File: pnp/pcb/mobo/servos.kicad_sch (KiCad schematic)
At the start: 3 parts, among them J15 SERVO1, J16 SERVO2, U7 SN74LVC2G34

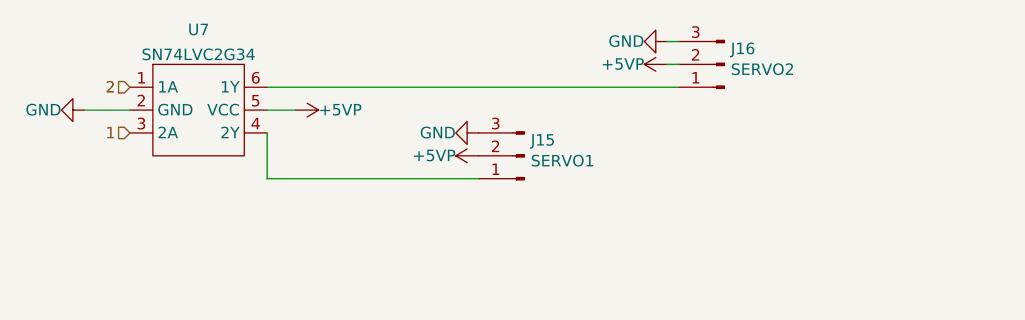
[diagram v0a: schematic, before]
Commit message: Mobo V4A Redesign
Some EMC improvements to schematics.
Reassigned MCU Pins for HW-PWM support.
Changes are still marked with text in the schematics.
Complete PCB Layout reworked
Status: Needs to be verified, and cleaned up a little, but DRC is running green.
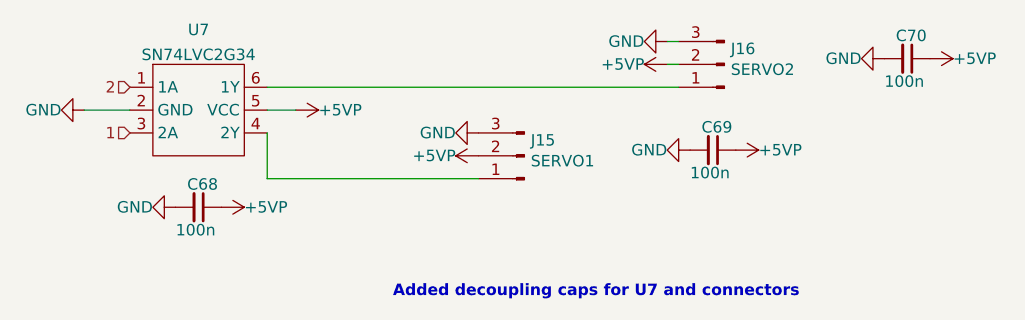
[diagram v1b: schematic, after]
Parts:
- added C68, C69, C70: 100n, Capacitor_SMD:C_0805_2012Metric, symbol Device:C_Small
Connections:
- net +5VP: now also C68.1, C69.1, C70.1
- net GND: now also C68.2, C69.2, C70.2
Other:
- note added: "Added decoupling caps for U7 and connectors"
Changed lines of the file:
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@@
   (title_block
     (title "LumenPnP Motherboard")
-    (date "2022-03-29")
+    (date "2022-09-09")
+    (rev "004A")
     (company "Opulo")
+    (comment 1 "Reengineered by Magpie")
   )
   (wire (pts (xy 119.38 108.585) (xy 142.875 108.585))
@@
   (wire (pts (xy 99.06 100.965) (xy 104.14 100.965))
     (stroke (width 0) (type default) (color 0 0 0 0))
+  )
+  (text "Added decoupling caps for U7 and connectors" (at 133.35 121.92 0)
+    (effects (font (size 1.27 1.27) (thickness 0.254) bold) (justify left bottom))
   )
   (hierarchical_label "1" (shape input) (at 104.14 103.505 180)
@@
     (effects (font (size 1.27 1.27)) (justify right))
   )
+  (symbol (lib_id "power:GND") (at 187.96 95.25 270) (unit 1)
+    (in_bom yes) (on_board yes)
+    (property "Reference" "#PWR030" (id 0) (at 181.61 95.25 0)
+      (effects (font (size 1.27 1.27)) hide)
+    )
+    (property "Value" "GND" (id 1) (at 185.42 95.25 90)
+      (effects (font (size 1.27 1.27)) (justify right))
+    )
+    (property "Footprint" "" (id 2) (at 187.96 95.25 0)
+      (effects (font (size 1.27 1.27)) hide)
+    )
+    (property "Datasheet" "" (id 3) (at 187.96 95.25 0)
+      (effects (font (size 1.27 1.27)) hide)
+    )
+    (pin "1")
+  )
   (symbol (lib_id "power:+5VP") (at 142.875 106.045 90) (unit 1)
     (in_bom yes) (on_board yes)
@@
     )
     (property "Datasheet" "" (id 3) (at 142.875 106.045 0)
+      (effects (font (size 1.27 1.27)) hide)
+    )
+    (pin "1")
+  )
+  (symbol (lib_id "power:+5VP") (at 171.45 105.41 270) (unit 1)
+    (in_bom yes) (on_board yes)
+    (property "Reference" "#PWR029" (id 0) (at 167.64 105.41 0)
+      (effects (font (size 1.27 1.27)) hide)
+    )
+    (property "Value" "+5VP" (id 1) (at 173.99 105.41 90)
+      (effects (font (size 1.27 1.27)) (justify left))
+    )
+    (property "Footprint" "" (id 2) (at 171.45 105.41 0)
+      (effects (font (size 1.27 1.27)) hide)
+    )
+    (property "Datasheet" "" (id 3) (at 171.45 105.41 0)
       (effects (font (size 1.27 1.27)) hide)
     )
@@
     (pin "1")
   )
+  (symbol (lib_id "power:GND") (at 166.37 105.41 270) (unit 1)
+    (in_bom yes) (on_board yes)
+    (property "Reference" "#PWR028" (id 0) (at 160.02 105.41 0)
+      (effects (font (size 1.27 1.27)) hide)
+    )
+    (property "Value" "GND" (id 1) (at 163.83 105.41 90)
+      (effects (font (size 1.27 1.27)) (justify right))
+    )
+    (property "Footprint" "" (id 2) (at 166.37 105.41 0)
+      (effects (font (size 1.27 1.27)) hide)
+    )
+    (property "Datasheet" "" (id 3) (at 166.37 105.41 0)
+      (effects (font (size 1.27 1.27)) hide)
+    )
+    (pin "1")
+  )
+  (symbol (lib_id "power:GND") (at 109.22 111.76 270) (unit 1)
+    (in_bom yes) (on_board yes)
+    (property "Reference" "#PWR026" (id 0) (at 102.87 111.76 0)
+      (effects (font (size 1.27 1.27)) hide)
+    )
+    (property "Value" "GND" (id 1) (at 106.68 111.76 90)
+      (effects (font (size 1.27 1.27)) (justify right))
+    )
+    (property "Footprint" "" (id 2) (at 109.22 111.76 0)
+      (effects (font (size 1.27 1.27)) hide)
+    )
+    (property "Datasheet" "" (id 3) (at 109.22 111.76 0)
+      (effects (font (size 1.27 1.27)) hide)
+    )
+    (pin "1")
+  )
+  (symbol (lib_id "Device:C_Small") (at 168.91 105.41 270) (unit 1)
+    (in_bom yes) (on_board yes)
+    (property "Reference" "C69" (id 0) (at 167.64 102.87 90)
+      (effects (font (size 1.27 1.27)) (justify left))
+    )
+    (property "Value" "100n" (id 1) (at 166.37 107.95 90)
+      (effects (font (size 1.27 1.27)) (justify left))
+    )
+    (property "Footprint" "Capacitor_SMD:C_0805_2012Metric" (id 2) (at 168.91 105.41 0)
+      (effects (font (size 1.27 1.27)) hide)
+    )
+    (property "Datasheet" "" (id 3) (at 168.91 105.41 0)
+      (effects (font (size 1.27 1.27)) hide)
+    )
+    (property "Digikey" "1276-1180-1-ND" (id 4) (at 168.91 105.41 0)
+      (effects (font (size 1.27 1.27)) hide)
+    )
+    (property "JLCPCB" "C49678" (id 5) (at 168.91 105.41 0)
+      (effects (font (size 1.27 1.27)) hide)
+    )
+    (property "LCSC" "C360619" (id 6) (at 168.91 105.41 0)
+      (effects (font (size 1.27 1.27)) hide)
+    )
+    (property "Mouser" "581-08055C104K" (id 7) (at 168.91 105.41 0)
+      (effects (font (size 1.27 1.27)) hide)
+    )
+    (pin "1")
+    (pin "2")
+  )
   (symbol (lib_id "power:GND") (at 163.83 93.345 270) (unit 1)
     (in_bom yes) (on_board yes)
@@
     (pin "1")
   )
+  (symbol (lib_id "power:+5VP") (at 114.3 111.76 270) (unit 1)
+    (in_bom yes) (on_board yes)
+    (property "Reference" "#PWR027" (id 0) (at 110.49 111.76 0)
+      (effects (font (size 1.27 1.27)) hide)
+    )
+    (property "Value" "+5VP" (id 1) (at 116.84 111.76 90)
+      (effects (font (size 1.27 1.27)) (justify left))
+    )
+    (property "Footprint" "" (id 2) (at 114.3 111.76 0)
+      (effects (font (size 1.27 1.27)) hide)
+    )
+    (property "Datasheet" "" (id 3) (at 114.3 111.76 0)
+      (effects (font (size 1.27 1.27)) hide)
+    )
+    (pin "1")
+  )
   (symbol (lib_id "power:+5VP") (at 163.83 95.885 90) (unit 1)
     (in_bom yes) (on_board yes)
@@
     (pin "1")
   )
+  (symbol (lib_id "Device:C_Small") (at 111.76 111.76 270) (unit 1)
+    (in_bom yes) (on_board yes)
+    (property "Reference" "C68" (id 0) (at 110.49 109.22 90)
+      (effects (font (size 1.27 1.27)) (justify left))
+    )
+    (property "Value" "100n" (id 1) (at 109.22 114.3 90)
+      (effects (font (size 1.27 1.27)) (justify left))
+    )
+    (property "Footprint" "Capacitor_SMD:C_0805_2012Metric" (id 2) (at 111.76 111.76 0)
+      (effects (font (size 1.27 1.27)) hide)
+    )
+    (property "Datasheet" "" (id 3) (at 111.76 111.76 0)
+      (effects (font (size 1.27 1.27)) hide)
+    )
+    (property "Digikey" "1276-1180-1-ND" (id 4) (at 111.76 111.76 0)
+      (effects (font (size 1.27 1.27)) hide)
+    )
+    (property "JLCPCB" "C49678" (id 5) (at 111.76 111.76 0)
+      (effects (font (size 1.27 1.27)) hide)
+    )
+    (property "LCSC" "C360619" (id 6) (at 111.76 111.76 0)
+      (effects (font (size 1.27 1.27)) hide)
+    )
+    (property "Mouser" "581-08055C104K" (id 7) (at 111.76 111.76 0)
+      (effects (font (size 1.27 1.27)) hide)
+    )
+    (pin "1")
+    (pin "2")
+  )
   (symbol (lib_id "Connector:Conn_01x03_Male") (at 170.18 95.885 180) (unit 1)
     (in_bom yes) (on_board yes)
@@
     (pin "3")
   )
+  (symbol (lib_id "power:+5VP") (at 193.04 95.25 270) (unit 1)
+    (in_bom yes) (on_board yes)
+    (property "Reference" "#PWR031" (id 0) (at 189.23 95.25 0)
+      (effects (font (size 1.27 1.27)) hide)
+    )
+    (property "Value" "+5VP" (id 1) (at 195.58 95.25 90)
+      (effects (font (size 1.27 1.27)) (justify left))
+    )
+    (property "Footprint" "" (id 2) (at 193.04 95.25 0)
+      (effects (font (size 1.27 1.27)) hide)
+    )
+    (property "Datasheet" "" (id 3) (at 193.04 95.25 0)
+      (effects (font (size 1.27 1.27)) hide)
+    )
+    (pin "1")
+  )
+  (symbol (lib_id "Device:C_Small") (at 190.5 95.25 270) (unit 1)
+    (in_bom yes) (on_board yes)
+    (property "Reference" "C70" (id 0) (at 189.23 92.71 90)
+      (effects (font (size 1.27 1.27)) (justify left))
+    )
+    (property "Value" "100n" (id 1) (at 187.96 97.79 90)
+      (effects (font (size 1.27 1.27)) (justify left))
+    )
+    (property "Footprint" "Capacitor_SMD:C_0805_2012Metric" (id 2) (at 190.5 95.25 0)
+      (effects (font (size 1.27 1.27)) hide)
+    )
+    (property "Datasheet" "" (id 3) (at 190.5 95.25 0)
+      (effects (font (size 1.27 1.27)) hide)
+    )
+    (property "Digikey" "1276-1180-1-ND" (id 4) (at 190.5 95.25 0)
+      (effects (font (size 1.27 1.27)) hide)
+    )
+    (property "JLCPCB" "C49678" (id 5) (at 190.5 95.25 0)
+      (effects (font (size 1.27 1.27)) hide)
+    )
+    (property "LCSC" "C360619" (id 6) (at 190.5 95.25 0)
+      (effects (font (size 1.27 1.27)) hide)
+    )
+    (property "Mouser" "581-08055C104K" (id 7) (at 190.5 95.25 0)
+      (effects (font (size 1.27 1.27)) hide)
+    )
+    (pin "1")
+    (pin "2")
+  )
 )

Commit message: Redesign finished
Completed Board redesign and adding more EMC improvements.
Changed all the part numbers to have a Mouser orderable design (except the JST connectors)
All outputs generated
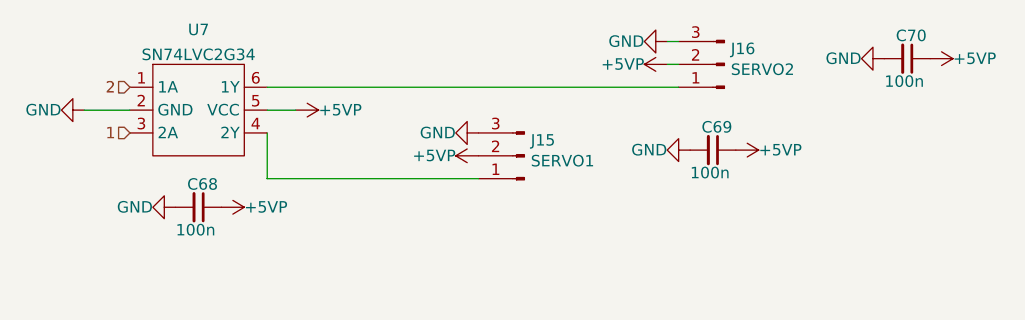
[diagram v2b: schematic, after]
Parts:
- C68, C69, C70: Digikey 1276-1180-1-ND -> (none); JLCPCB C49678 -> (none); LCSC C360619 -> (none); Mouser 581-08055C104K -> 710-885012207098
- J15, J16: JLCPCB C2316 -> (none); LCSC C2316 -> (none); Mouser (none) -> Digikey
- U7: Mouser (none) -> 595-SN74LVC2G34DBVR
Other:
- note removed: "Added decoupling caps for U7 and connectors"
- company: Opulo -> Opulo.io
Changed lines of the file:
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@@
   (title_block
     (title "LumenPnP Motherboard")
-    (date "2022-09-09")
-    (rev "004A")
-    (company "Opulo")
+    (date "2022-10-06")
+    (rev "04A")
+    (company "Opulo.io")
     (comment 1 "Reengineered by Magpie")
   )
@@
   (wire (pts (xy 99.06 100.965) (xy 104.14 100.965))
     (stroke (width 0) (type default) (color 0 0 0 0))
-  )
-  (text "Added decoupling caps for U7 and connectors" (at 133.35 121.92 0)
-    (effects (font (size 1.27 1.27) (thickness 0.254) bold) (justify left bottom))
   )
   (hierarchical_label "1" (shape input) (at 104.14 103.505 180)
@@
       (effects (font (size 1.27 1.27)) hide)
     )
+    (property "Mouser" "595-SN74LVC2G34DBVR" (id 4) (at 111.76 106.045 0)
+      (effects (font (size 1.27 1.27)) hide)
+    )
     (pin "1")
     (pin "2")
@@
       (effects (font (size 1.27 1.27)) hide)
     )
-    (property "Digikey" "1276-1180-1-ND" (id 4) (at 168.91 105.41 0)
-      (effects (font (size 1.27 1.27)) hide)
-    )
-    (property "JLCPCB" "C49678" (id 5) (at 168.91 105.41 0)
-      (effects (font (size 1.27 1.27)) hide)
-    )
-    (property "LCSC" "C360619" (id 6) (at 168.91 105.41 0)
-      (effects (font (size 1.27 1.27)) hide)
-    )
-    (property "Mouser" "581-08055C104K" (id 7) (at 168.91 105.41 0)
+    (property "Digikey" "" (id 4) (at 168.91 105.41 0)
+      (effects (font (size 1.27 1.27)) hide)
+    )
+    (property "JLCPCB" "" (id 5) (at 168.91 105.41 0)
+      (effects (font (size 1.27 1.27)) hide)
+    )
+    (property "LCSC" "" (id 6) (at 168.91 105.41 0)
+      (effects (font (size 1.27 1.27)) hide)
+    )
+    (property "Mouser" "710-885012207098" (id 7) (at 168.91 105.41 0)
       (effects (font (size 1.27 1.27)) hide)
     )
@@
       (effects (font (size 1.27 1.27)) hide)
     )
-    (property "LCSC" "C2316" (id 4) (at 147.955 106.045 0)
-      (effects (font (size 1.27 1.27)) hide)
-    )
-    (property "JLCPCB" "C2316" (id 5) (at 147.955 106.045 0)
+    (property "LCSC" "" (id 4) (at 147.955 106.045 0)
+      (effects (font (size 1.27 1.27)) hide)
+    )
+    (property "JLCPCB" "" (id 5) (at 147.955 106.045 0)
       (effects (font (size 1.27 1.27)) hide)
     )
@@
       (effects (font (size 1.27 1.27)) hide)
     )
+    (property "Mouser" "Digikey" (id 7) (at 147.955 106.045 0)
+      (effects (font (size 1.27 1.27)) hide)
+    )
     (pin "1")
     (pin "2")
@@
       (effects (font (size 1.27 1.27)) hide)
     )
-    (property "Digikey" "1276-1180-1-ND" (id 4) (at 111.76 111.76 0)
-      (effects (font (size 1.27 1.27)) hide)
-    )
-    (property "JLCPCB" "C49678" (id 5) (at 111.76 111.76 0)
-      (effects (font (size 1.27 1.27)) hide)
-    )
-    (property "LCSC" "C360619" (id 6) (at 111.76 111.76 0)
-      (effects (font (size 1.27 1.27)) hide)
-    )
-    (property "Mouser" "581-08055C104K" (id 7) (at 111.76 111.76 0)
+    (property "Digikey" "" (id 4) (at 111.76 111.76 0)
+      (effects (font (size 1.27 1.27)) hide)
+    )
+    (property "JLCPCB" "" (id 5) (at 111.76 111.76 0)
+      (effects (font (size 1.27 1.27)) hide)
+    )
+    (property "LCSC" "" (id 6) (at 111.76 111.76 0)
+      (effects (font (size 1.27 1.27)) hide)
+    )
+    (property "Mouser" "710-885012207098" (id 7) (at 111.76 111.76 0)
       (effects (font (size 1.27 1.27)) hide)
     )
@@
       (effects (font (size 1.27 1.27)) hide)
     )
-    (property "LCSC" "C2316" (id 4) (at 170.18 95.885 0)
-      (effects (font (size 1.27 1.27)) hide)
-    )
-    (property "JLCPCB" "C2316" (id 5) (at 170.18 95.885 0)
+    (property "LCSC" "" (id 4) (at 170.18 95.885 0)
+      (effects (font (size 1.27 1.27)) hide)
+    )
+    (property "JLCPCB" "" (id 5) (at 170.18 95.885 0)
       (effects (font (size 1.27 1.27)) hide)
     )
@@
       (effects (font (size 1.27 1.27)) hide)
     )
+    (property "Mouser" "Digikey" (id 7) (at 170.18 95.885 0)
+      (effects (font (size 1.27 1.27)) hide)
+    )
     (pin "1")
     (pin "2")
@@
       (effects (font (size 1.27 1.27)) hide)
     )
-    (property "Digikey" "1276-1180-1-ND" (id 4) (at 190.5 95.25 0)
-      (effects (font (size 1.27 1.27)) hide)
-    )
-    (property "JLCPCB" "C49678" (id 5) (at 190.5 95.25 0)
-      (effects (font (size 1.27 1.27)) hide)
-    )
-    (property "LCSC" "C360619" (id 6) (at 190.5 95.25 0)
-      (effects (font (size 1.27 1.27)) hide)
-    )
-    (property "Mouser" "581-08055C104K" (id 7) (at 190.5 95.25 0)
-      (effects (font (size 1.27 1.27)) hide)
-    )
+    (property "Digikey" "" (id 4) (at 190.5 95.25 0)
+      (effects (font (size 1.27 1.27)) hide)
+    )
+    (property "JLCPCB" "" (id 5) (at 190.5 95.25 0)
+      (effects (font (size 1.27 1.27)) hide)
+    )
+    (property "LCSC" "" (id 6) (at 190.5 95.25 0)
+      (effects (font (size 1.27 1.27)) hide)
+    )
+    (property "Mouser" "710-885012207098" (id 7) (at 190.5 95.25 0)
+      (effects (font (size 1.27 1.27)) hide)
+    )
